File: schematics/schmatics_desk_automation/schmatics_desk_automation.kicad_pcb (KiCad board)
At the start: 2 copper layers, 122.5 x 110 mm, 12 parts, among them SW1 BT_UP, SW3 BT_DOWN, U1 L298N

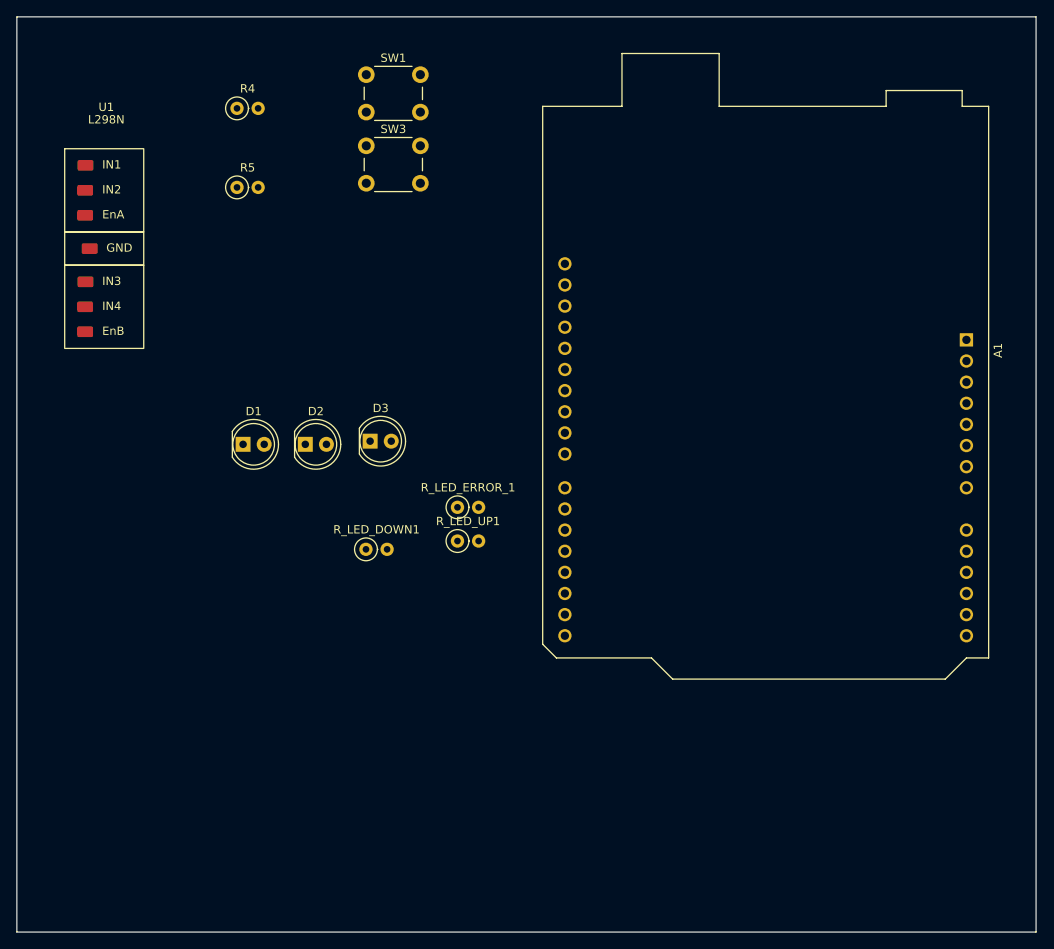
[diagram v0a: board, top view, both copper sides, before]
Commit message: Remove autosave lock file for schematics desk automation
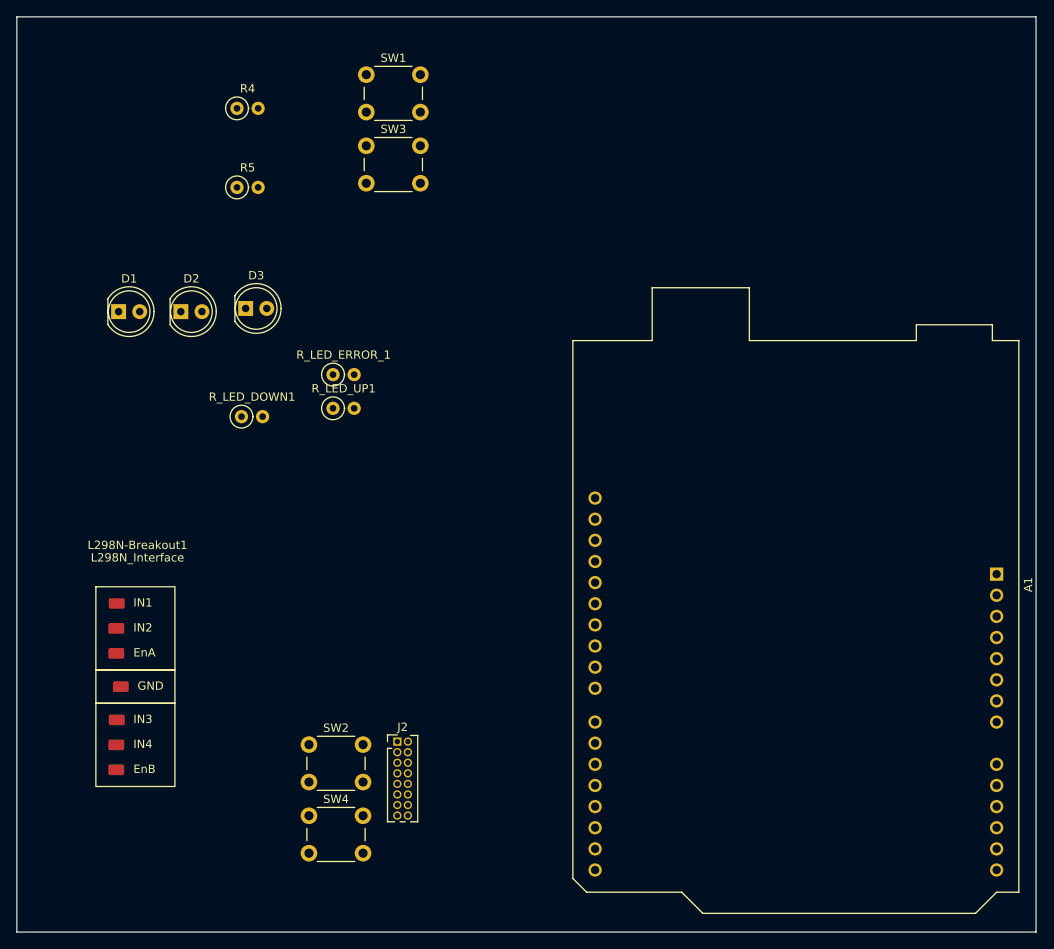
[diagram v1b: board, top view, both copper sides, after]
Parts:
- removed U1: L298N, DeskAutomation:L298N Interface
- added J2: Conn_01x15_MountingPin, Connector_PinHeader_1.27mm:PinHeader_2x08_P1.27mm_Vertical, F.Cu at (188.2, 127.1)
- added L298N-Breakout1: L298N_Interface, DeskAutomation:L298N Interface, F.Cu at (157.0, 104.0)
- added SW2: Lower Limit, Button_Switch_THT:SW_PUSH_6mm_H5mm, F.Cu at (177.6, 127.5)
- added SW4: Uppr Limit, Button_Switch_THT:SW_PUSH_6mm_H5mm, F.Cu at (177.6, 136.0)
- moved A1 28.4 mm to (260.3, 107.0)
- moved D3 21.9 mm to (170.0, 75.0)
- moved R_LED_DOWN1 21.9 mm to (169.5, 88.0)
- moved R_LED_ERROR_1 21.9 mm to (180.5, 83.0)
- moved R_LED_UP1 21.9 mm to (180.5, 87.0)
- moved D1 21.9 mm to (154.7, 75.4)
- moved D2 21.9 mm to (162.2, 75.4)
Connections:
- D1 pad 2: Net-(D1-A) -> GND
- D2 pad 2: Net-(D1-A) -> GND
- D3 pad 2: Net-(D1-A) -> GND
- R4 pad 2: Net-(A1-GND-Pad29) -> GND
- R5 pad 2: Net-(A1-GND-Pad29) -> GND
- R_LED_ERROR_1 pad 1: LED_ERROR -> GND
